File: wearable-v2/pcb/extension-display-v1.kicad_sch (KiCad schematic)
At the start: 19 parts, among them J9 HERALD_V2_CONN_PLUG, U10 ATmega328PB-M, U13 LM386, U16 DRV2605LDGS, U7 MX25R8035FZxxx0, Y2 16Mhz

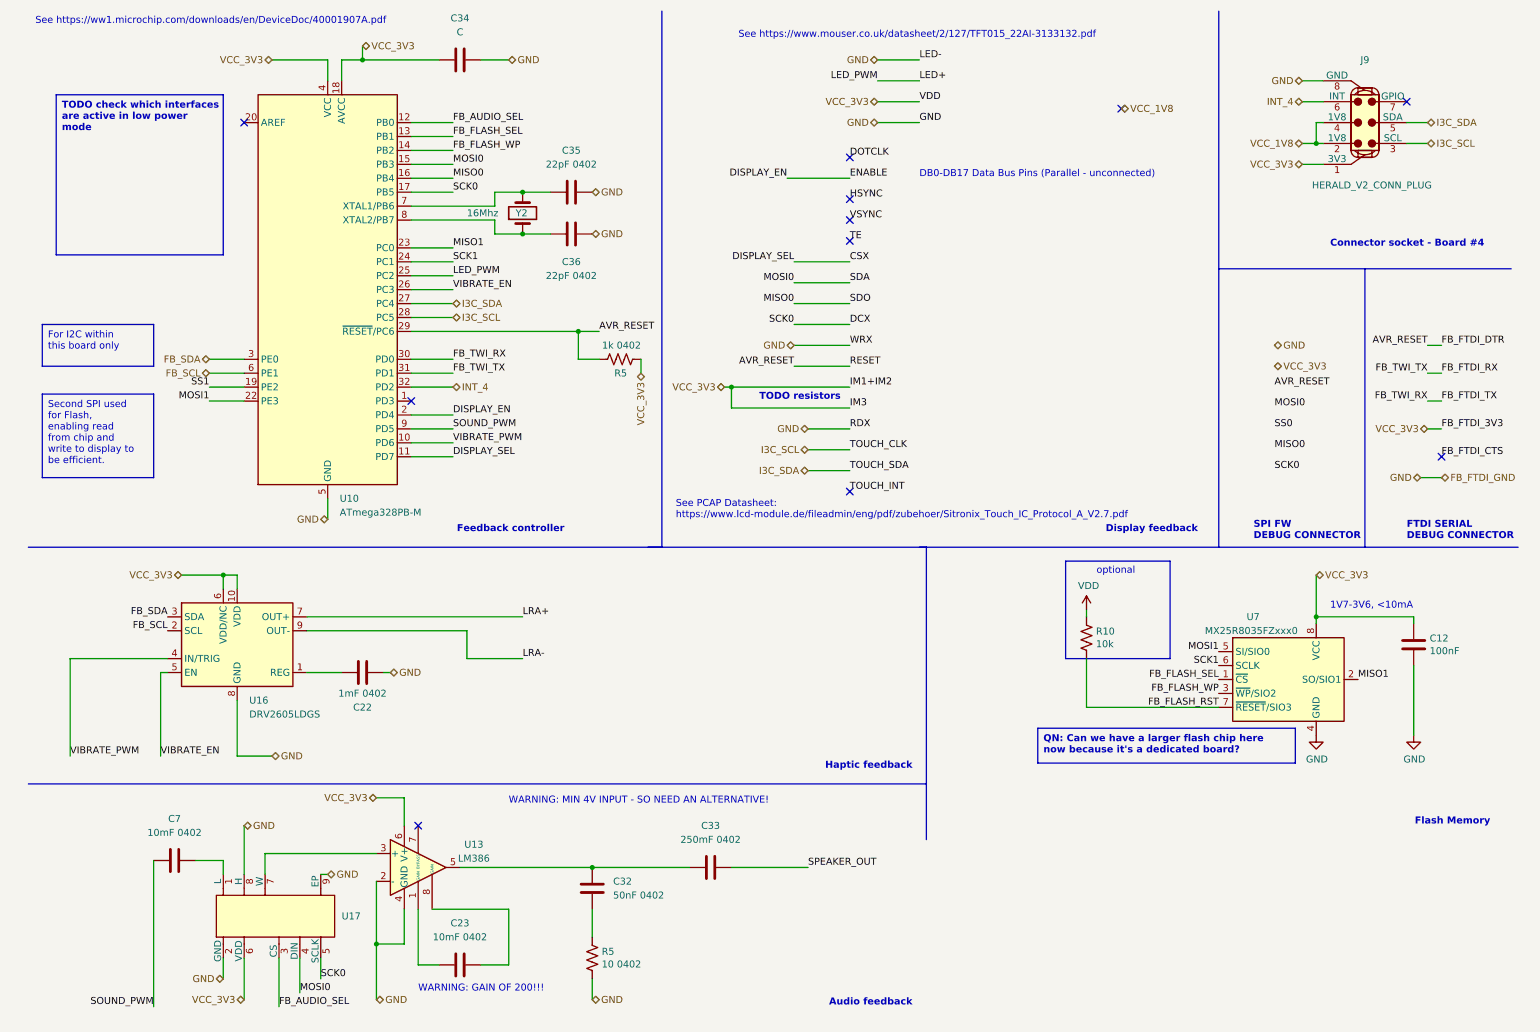
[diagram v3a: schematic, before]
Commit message: Added MPN and footprints to display components
Signed-off-by: Adam Fowler <adam@adamfowler.org>
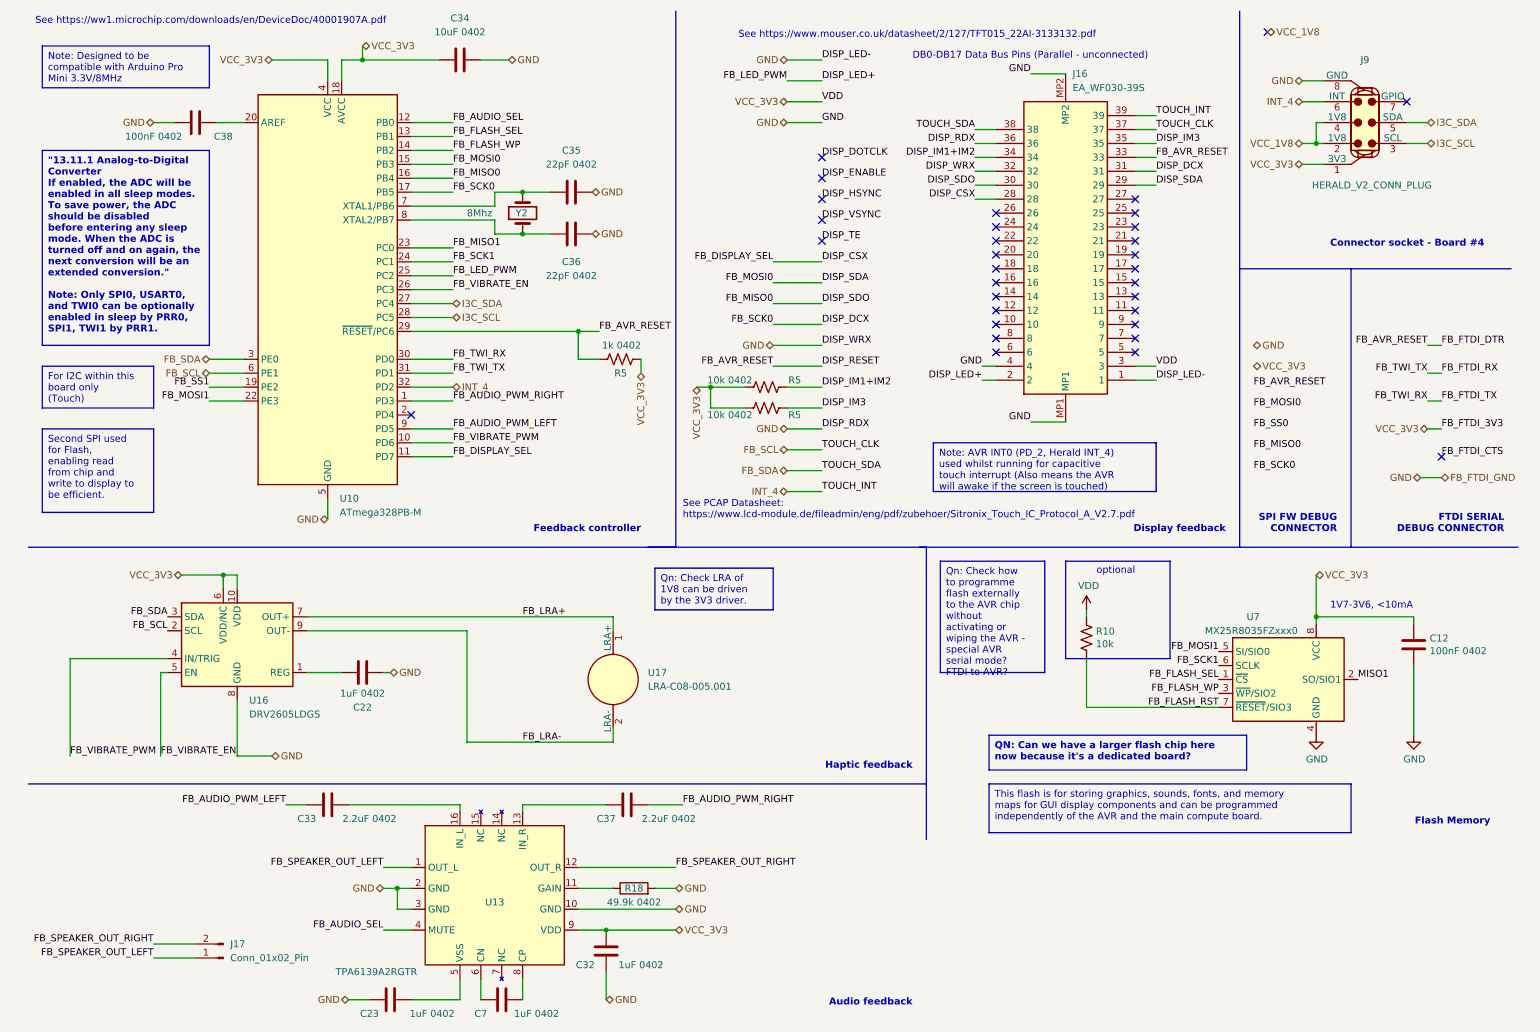
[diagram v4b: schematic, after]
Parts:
- removed R5: 10 0402, Resistor_SMD:R_0402_1005Metric, symbol Device:R_US
- removed U13: LM386, symbol Amplifier_Audio:LM386
- removed U17: ~, Package_DFN_QFN:DFN-8-1EP_2x2mm_P0.5mm_EP1.05x1.75mm, symbol Herald_Extras:MAX5394
- added C37: 2.2uF 0402, Capacitor_SMD:C_0402_1005Metric, symbol Device:C
- added C38: 100nF 0402, Capacitor_SMD:C_0402_1005Metric, symbol Device:C
- added J16: EA_WF030-39S, Herald:EAWF03039S, symbol Herald_Extras:EA_WF030-39S
- added J17: Conn_01x02_Pin, Connector_JST:JST_SUR_SM02B-SURS-TF_1x02-1MP_P0.80mm_Horizontal, symbol Connector:Conn_01x02_Pin
- added R18: 49.9k 0402, Resistor_SMD:R_0402_1005Metric, symbol Device:R
- added R5 (x2): 10k 0402, Resistor_SMD:R_0402_1005Metric, symbol Device:R_US
- added U13: TPA6139A2RGTR, Package_DFN_QFN:TQFN-16-1EP_3x3mm_P0.5mm_EP1.6x1.6mm, symbol Herald_Extras:TPA6139A2
- added U17: LRA-C08-005.001, symbol Herald_Extras:LRA-C08-005.001
- C12: value 100nF -> 100nF 0402
- C22: value 1mF 0402 -> 1uF 0402; footprint (none) -> Capacitor_SMD:C_0402_1005Metric; MPN (none) -> GRM155R70J105KA12J
- C23, C7: value 10mF 0402 -> 1uF 0402; footprint (none) -> Capacitor_SMD:C_0402_1005Metric; MPN (none) -> GRM155R70J105KA12J
- C32: value 50nF 0402 -> 1uF 0402; footprint (none) -> Capacitor_SMD:C_0402_1005Metric; MPN (none) -> GRM155R70J105KA12J
- C33: value 250mF 0402 -> 2.2uF 0402; footprint (none) -> Capacitor_SMD:C_0402_1005Metric; MPN (none) -> GRM155C80J225KE95D
- C34: value C -> 10uF 0402; footprint (none) -> Capacitor_SMD:C_0402_1005Metric; MPN (none) -> GRM155R60J106ME15D
- C35, C36: footprint (none) -> Capacitor_SMD:C_0402_1005Metric; MPN (none) -> C0402C220K5GAC7867
- R5: MPN RK73H1ETTP1005F -> CRCW04021K00FKEDC
- U16: MPN (none) -> DRV2605LDGS
- Y2: value 16Mhz -> 8Mhz; footprint (none) -> Crystal:Crystal_SMD_5032-2Pin_5.0x3.2mm; MPN (none) -> WTL5G60390VH; Manufacturer (none) -> WTL
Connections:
- net FB_AUDIO_SEL: now also U13.4 (MUTE)
- net FB_SCL: now also J16.37
- net FB_SDA: now also J16.38
- net GND: now also C23.2, C32.2, C38.1, J16.1, J16.32, J16.36, J16.4, J16.MP1, J16.MP2, R18.2, U13.10 (GND), U13.2 (GND), U13.3 (GND)
- net INT_4: now also J16.39
- net MISO1: no longer U10.23 (PC0)
- net VDD: now also C32.1, J16.3, R5.1, R5.1, U13.9 (VDD)
- net at C7.2: now also U13.6 (CN)
- net at C23.1: now also U13.5 (VSS)
- net FB_AUDIO_PWM_LEFT: now reaches C33.2
- net FB_AUDIO_PWM_LEFT: now also U10.9 (PD5); no longer C32.1
- net FB_AUDIO_PWM_RIGHT: now reaches U10.1 (PD3)
- net FB_AUDIO_PWM_RIGHT: now also C37.1
- net at U10.20 (AREF): now also C38.2
- net AVR_RESET renamed DISP_RESET
- net DISP_RESET: now also J16.33
- net CSX renamed DISP_CSX
- net DISP_CSX: now also J16.28
- net DCX renamed DISP_DCX
- net DISP_DCX: now also J16.31
- net DISPLAY_EN: no longer names the net of U10.2 (PD4)
- net LED+ renamed DISP_LED+
- net DISP_LED+: now also J16.2
- net LRA+ renamed FB_LRA+
- net FB_LRA+: now also U17.1 (LRA+)
- net LRA- renamed FB_LRA-
- net FB_LRA-: now also U17.2 (LRA-)
- net MISO0 renamed DISP_SDO
- net DISP_SDO: now also J16.30
- net MOSI0 renamed DISP_SDA
- net DISP_SDA: now also J16.29
- net MOSI1 renamed FB_MOSI1
- net SCK1 renamed FB_SCK1
- net SOUND_PWM: no longer names the net of C7.1
- net SOUND_PWM: now also U13.8 (CP); no longer U10.9 (PD5)
- net SPEAKER_OUT: no longer names the net of C33.1
- net SPEAKER_OUT: now also U13.16 (IN_L)
- net SS1 renamed FB_SS1
- net VIBRATE_EN renamed FB_VIBRATE_EN
- net VIBRATE_PWM renamed FB_VIBRATE_PWM
- new net: R18.1, U13.11 (GAIN)
- new net: C37.2, U13.13 (IN_R)
- new net DISP_IM1+IM2: J16.34, R5.2
- new net DISP_IM3: J16.35, R5.2
- new net FB_MISO1: U10.23 (PC0)
- new net FB_SPEAKER_OUT_LEFT: J17.1 (Pin_1), U13.1 (OUT_L)
- new net FB_SPEAKER_OUT_RIGHT: J17.2 (Pin_2), U13.12 (OUT_R)
- no-connect marks 11 -> 32
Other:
- note removed: "TODO resistors"
- note removed: "WARNING: GAIN OF 200!!!"
- note removed: "WARNING: MIN 4V INPUT - SO NEED AN ALTERNATIVE!"

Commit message: Display board physical layout improvements
Signed-off-by: Adam Fowler <adam@adamfowler.org>
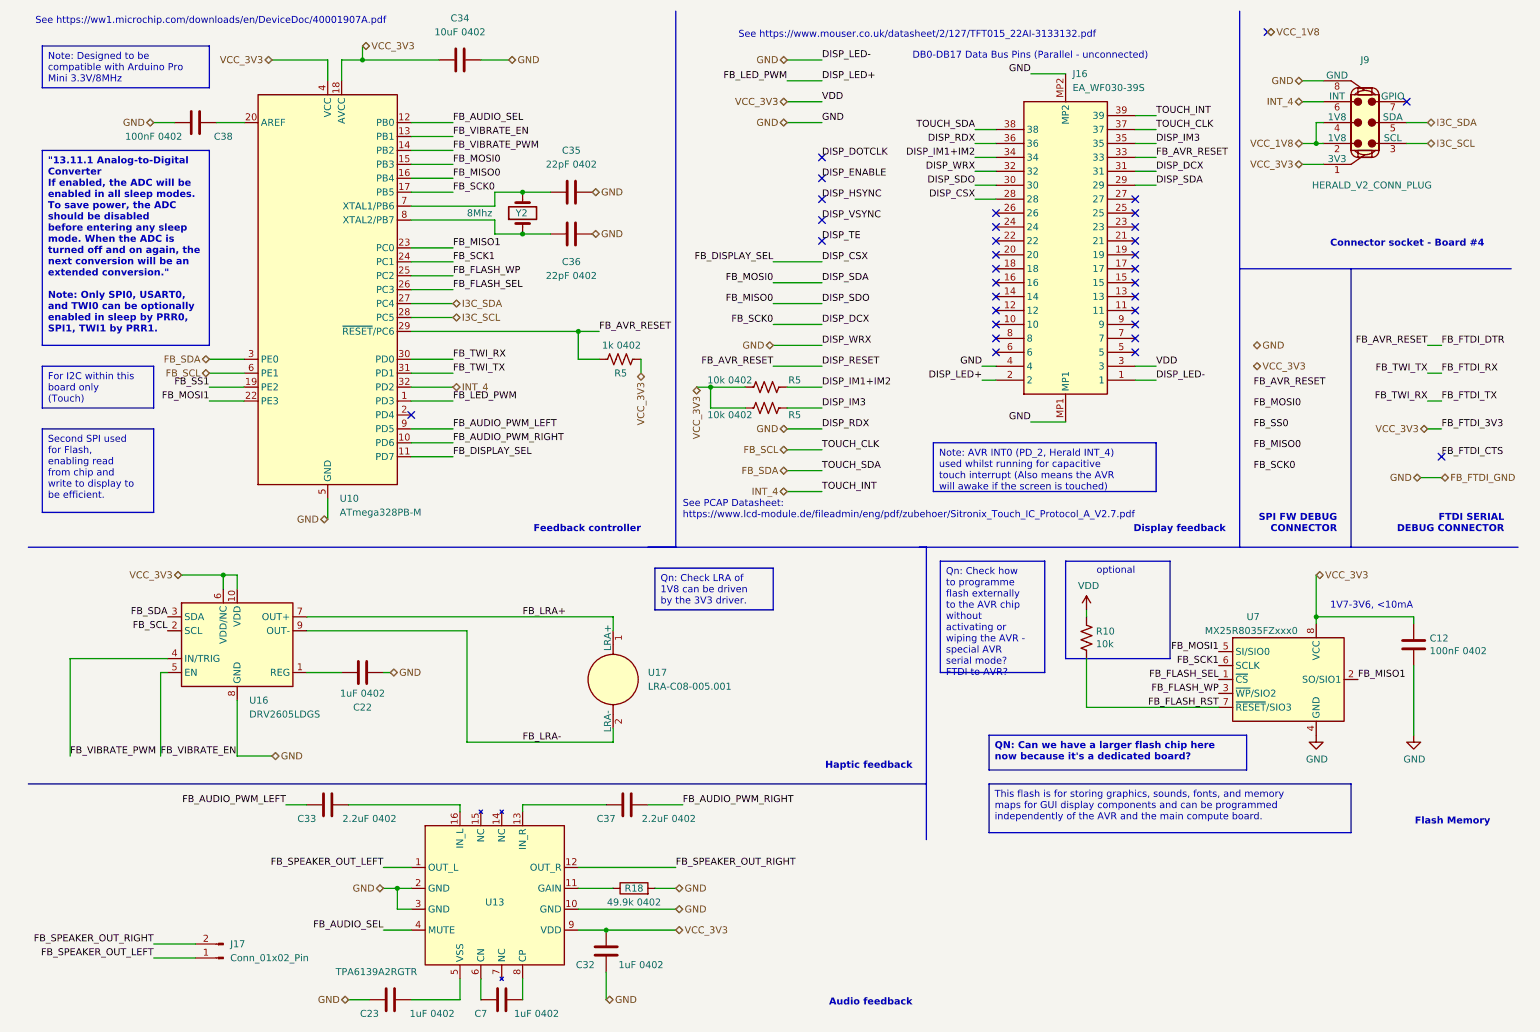
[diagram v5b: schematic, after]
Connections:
- net MISO1 is gone; now on net FB_MISO1: U7.2 (SO/SIO1)
- net DISP_LED+: now also U10.1 (PD3); no longer U10.25 (PC2)
- net FB_AUDIO_PWM_RIGHT: now also U10.10 (PD6); no longer U10.1 (PD3)
- net FB_FLASH_SEL: now also U10.26 (PC3); no longer U10.13 (PB1)
- net FB_FLASH_WP: now also U10.25 (PC2); no longer U10.14 (PB2)
- net FB_VIBRATE_EN: now also U10.13 (PB1); no longer U10.26 (PC3)
- net FB_VIBRATE_PWM: now also U10.14 (PB2); no longer U10.10 (PD6)

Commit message: Confirmed display board connectors
Signed-off-by: Adam Fowler <adam@adamfowler.org>
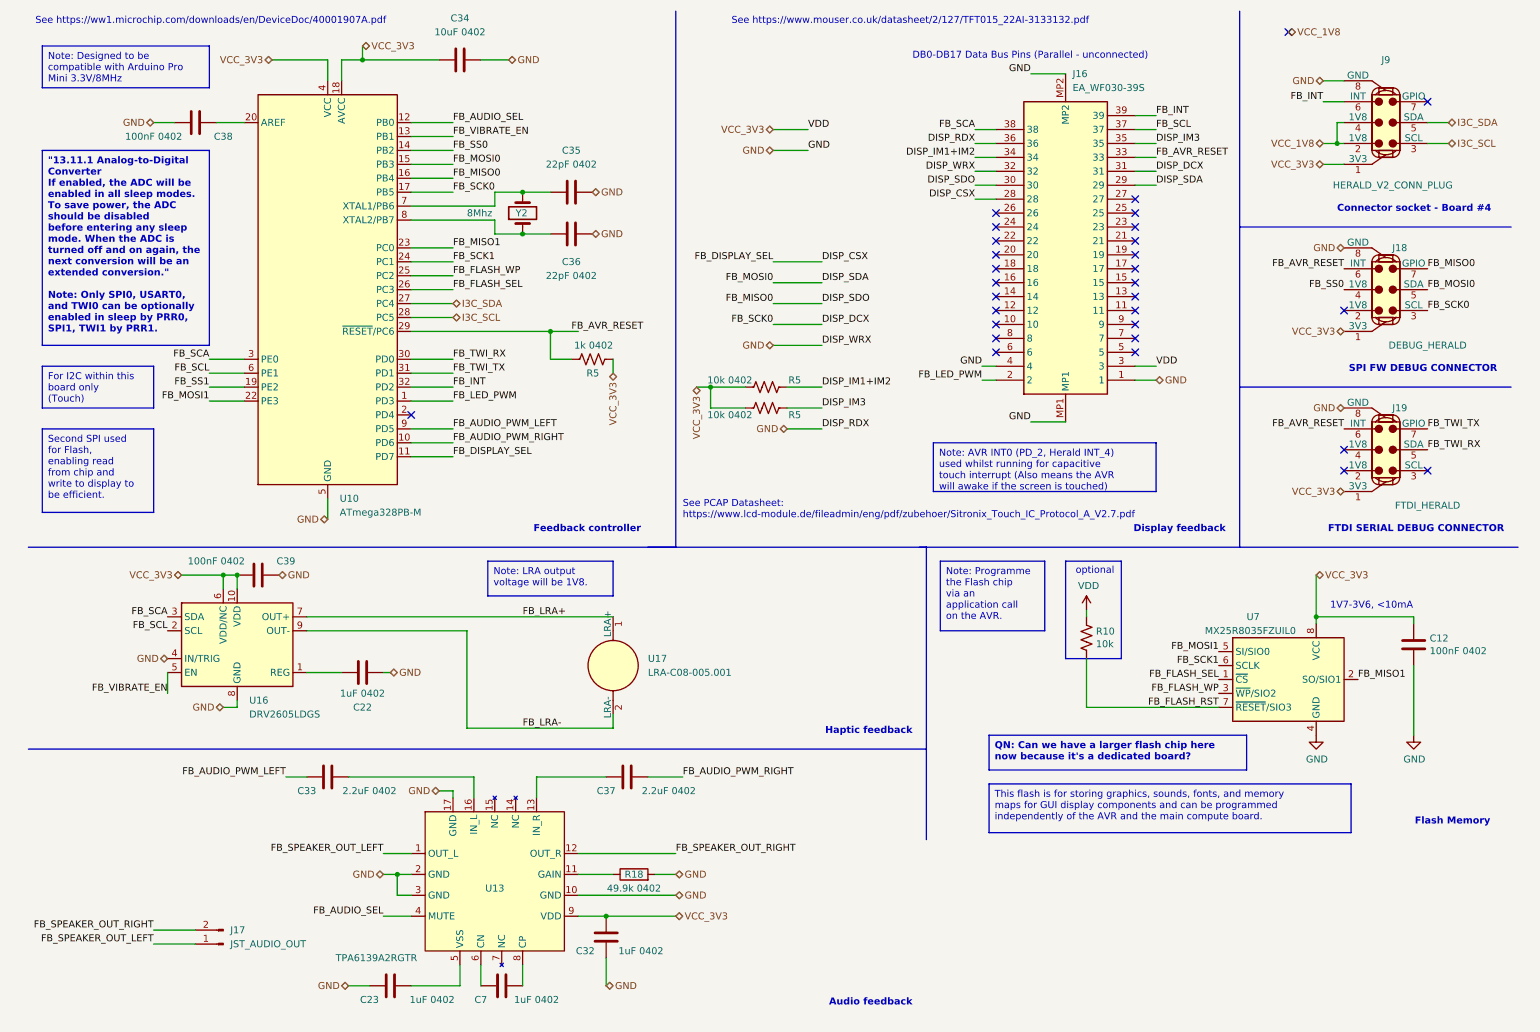
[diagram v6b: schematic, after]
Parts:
- added C39: 100nF 0402, Capacitor_SMD:C_0402_1005Metric, symbol Device:C
- added J18: DEBUG_HERALD, Herald:HERALD_V2_CONN_PORT, symbol Herald_Extras:HERALD_V2_CONN_PLUG
- added J19: FTDI_HERALD, Herald:HERALD_V2_CONN_PORT, symbol Herald_Extras:HERALD_V2_CONN_PLUG
- J17: value Conn_01x02_Pin -> JST_AUDIO_OUT
- J9: footprint (none) -> Herald:HERALD_V2_CONN_PORT
- U7: value MX25R8035FZxxx0 -> MX25R8035FZUIL0
- Y2: footprint Crystal:Crystal_SMD_5032-2Pin_5.0x3.2mm -> Crystal:Crystal_SMD_3225-4Pin_3.2x2.5mm; MPN WTL5G60390VH -> CG04874-8M; Manufacturer WTL -> NDK America, Inc.
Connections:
- net DISP_DCX: now also J18.3 (SCL)
- net DISP_SDA: now also J18.5 (SDA)
- net DISP_SDO: now also J18.7 (GPIO)
- net FB_SS0: now also U10.14 (PB2), J18.4 (1V8)
- net GND: now also U13.17 (GND), U16.4 (IN/TRIG), C39.2, J18.8 (GND), J19.8 (GND)
- net VDD: now also C39.1, J18.1 (3V3), J19.1 (3V3)
- net DISP_LED+ renamed FB_LED_PWM
- net DISP_RESET renamed FB_AVR_RESET
- net FB_AVR_RESET: now also J18.6 (INT), J19.6 (INT)
- net FB_FTDI_RX renamed FB_TWI_TX
- net FB_TWI_TX: now also J19.7 (GPIO)
- net FB_FTDI_TX renamed FB_TWI_RX
- net FB_TWI_RX: now also J19.5 (SDA)
- net FB_SDA renamed FB_SCA
- removed net FB_VIBRATE_PWM: U10.14 (PB2), U16.4 (IN/TRIG)
- net INT_4 renamed FB_INT
- no-connect marks 32 -> 30
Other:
- moved on the sheet: C23, C32, C33, C37, C7, J17, J9, R18, R5, U17

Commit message: Upgraded flash and corrected XIF placement
Signed-off-by: Adam Fowler <adam@adamfowler.org>
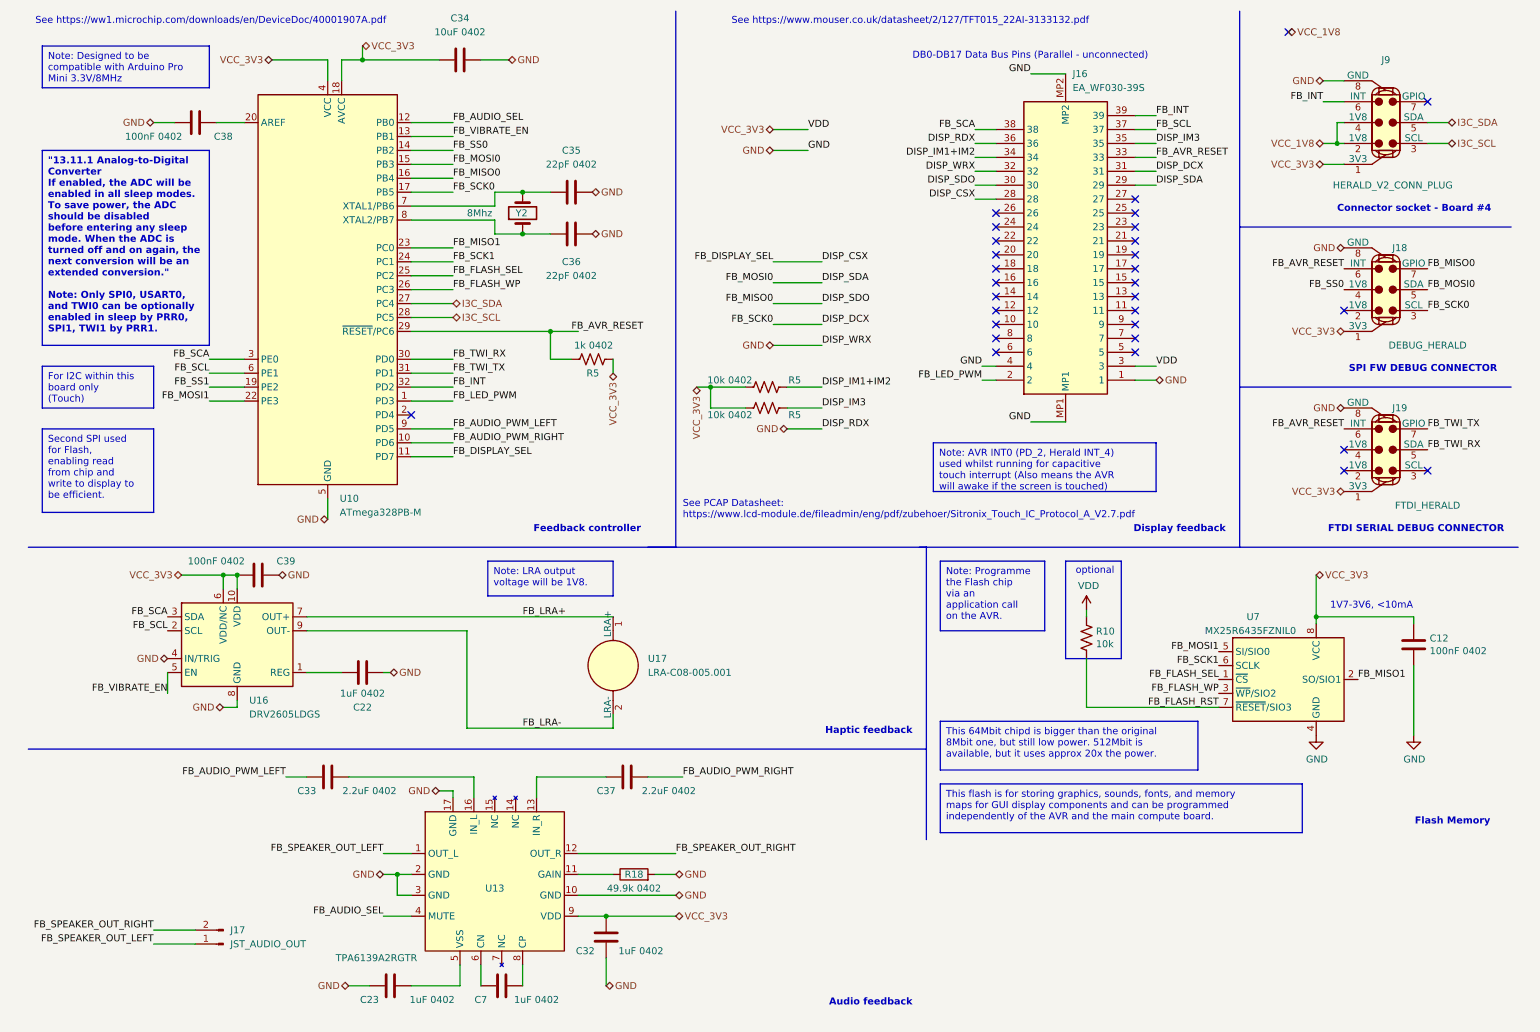
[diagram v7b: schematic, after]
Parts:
- U7: value MX25R8035FZUIL0 -> MX25R6435FZNIL0; footprint Herald:USON-8-1EP_2x3mm_P0.5mm_EP0.25x1.65mm -> Package_SON:WSON-8-1EP_6x5mm_P1.27mm_EP3.4x4mm; MPN MX25R8035FZUIL0 -> MX25R6435FZNIL0
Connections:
- net FB_FLASH_SEL: now also U10.25 (PC2); no longer U10.26 (PC3)
- net FB_FLASH_WP: now also U10.26 (PC3); no longer U10.25 (PC2)
